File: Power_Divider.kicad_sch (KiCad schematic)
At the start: 31 parts, among them J8 Molex 73251-1153, J9 2118714-2, P10 CONUFL001-SMD-T, P11 CONUFL001-SMD-T, P12 CONUFL001-SMD-T, P9 CONUFL001-SMD-T, Q2 BSS138, U25 QPL9547, U26 RBP-140+

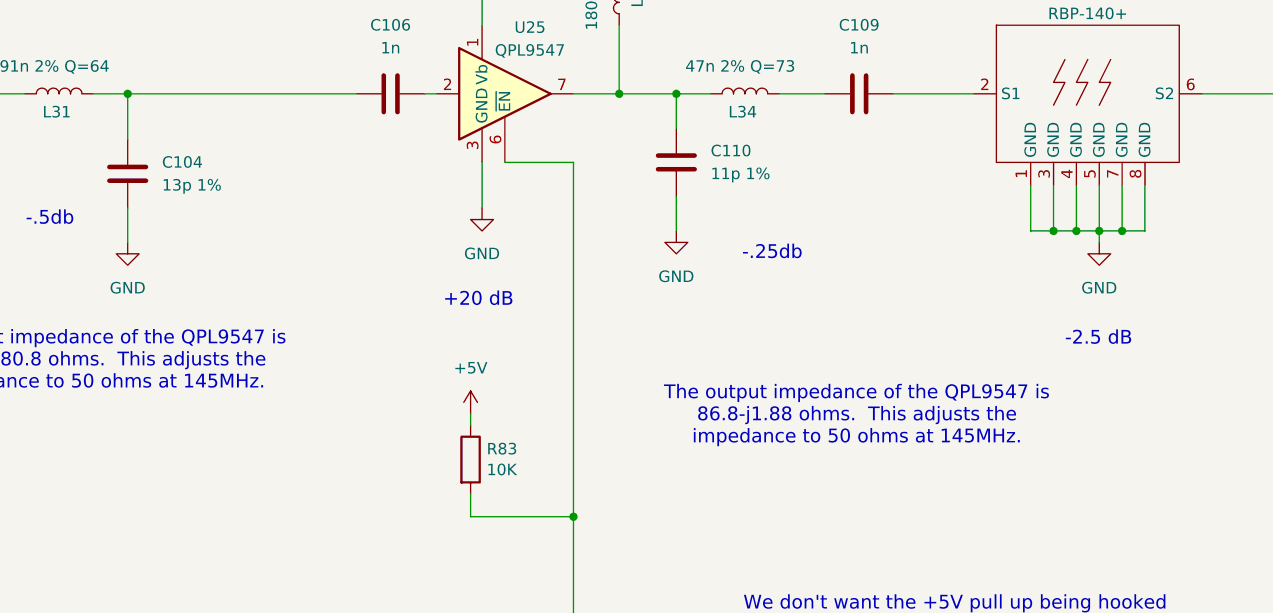
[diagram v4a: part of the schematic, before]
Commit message: More work on the LNA/PA impedance matchers
Did some simulations, found some issues.

Signed-off-by: Corey Minyard <corey@minyard.net>
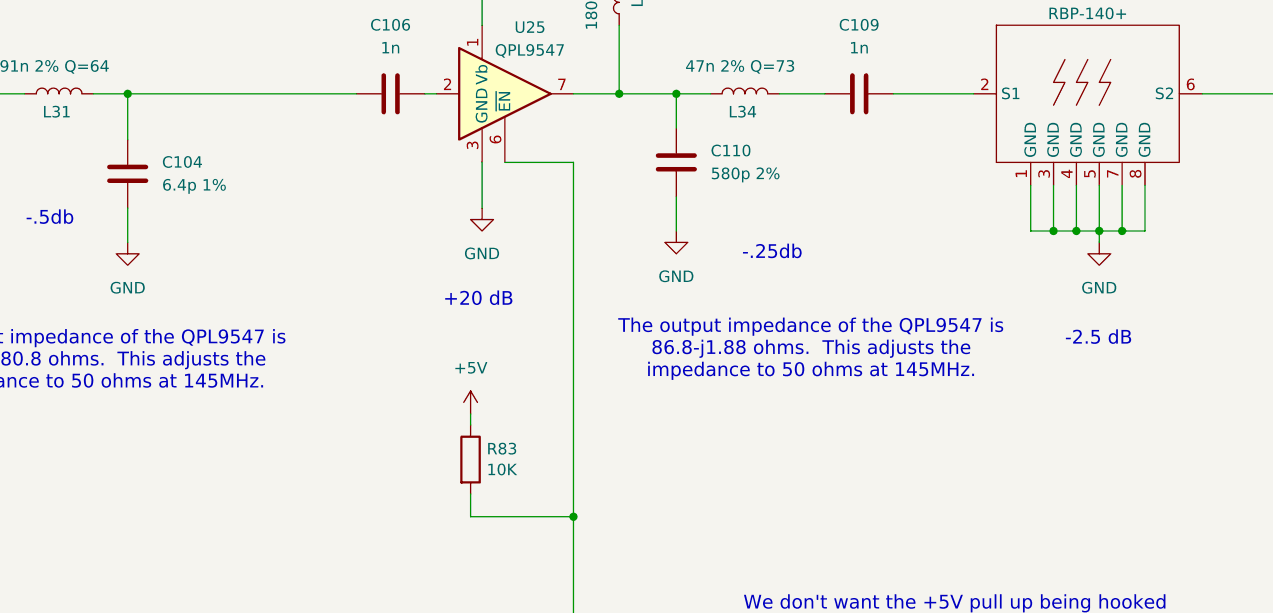
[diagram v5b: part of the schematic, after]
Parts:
- C104: value 13p 1% -> 6.4p 1%
- C110: value 11p 1% -> 580p 2%
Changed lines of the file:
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@@
 	(text "The output impedance of the QPL9547 is\n86.8-j1.88 ohms.  This adjusts the\nimpedance to 50 ohms at 145MHz."
 		(exclude_from_sim no)
-		(at 223.266 179.324 0)
+		(at 218.186 171.958 0)
 		(effects
 			(font
@@
 			)
 		)
-		(property "Value" "13p 1%"
+		(property "Value" "6.4p 1%"
 			(at 146.05 153.6699 0)
 			(effects
@@
 			)
 		)
-		(property "Value" "11p 1%"
+		(property "Value" "580p 2%"
 			(at 207.01 152.3999 0)
 			(effects

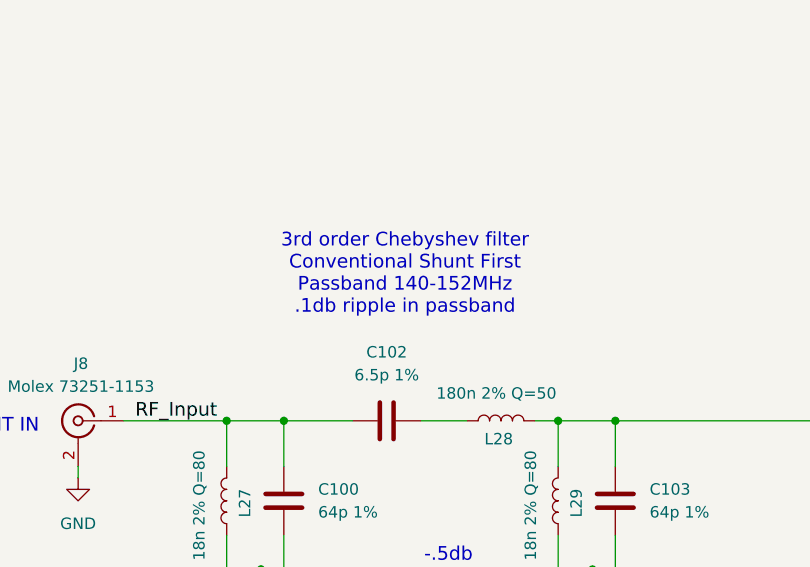
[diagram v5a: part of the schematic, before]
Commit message: Minor adjustments to values and impedance match simulation
Signed-off-by: Corey Minyard <corey@minyard.net>
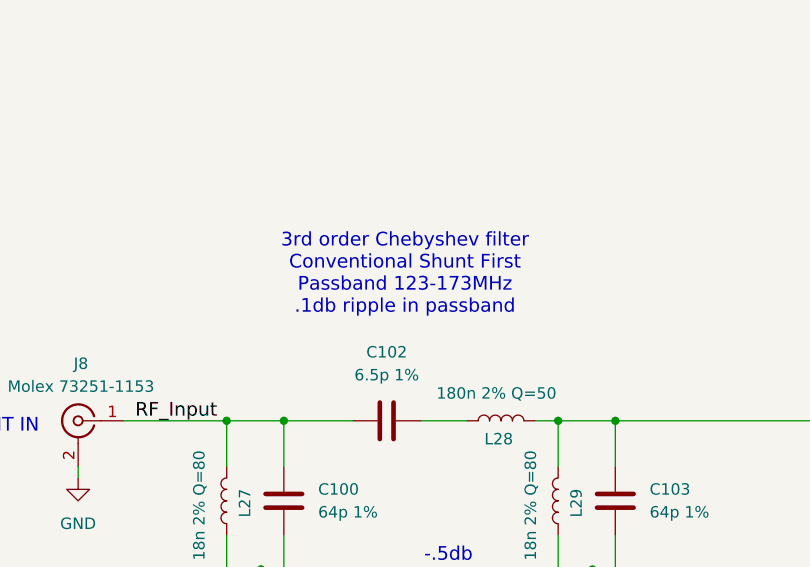
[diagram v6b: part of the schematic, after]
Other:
- note added: "3rd order Chebyshev filter Conventional Shunt First Passband 123-173MHz .1db ripple in passband"
- note removed: "3rd order Chebyshev filter Conventional Shunt First Passband 140-152MHz .1db ripple in passband"
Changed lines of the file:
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@@
 		)
 	)
-	(text "3rd order Chebyshev filter\nConventional Shunt First\nPassband 140-152MHz\n.1db ripple in passband\n"
+	(text "3rd order Chebyshev filter\nConventional Shunt First\nPassband 123-173MHz\n.1db ripple in passband\n"
 		(exclude_from_sim no)
 		(at 82.042 127.254 0)

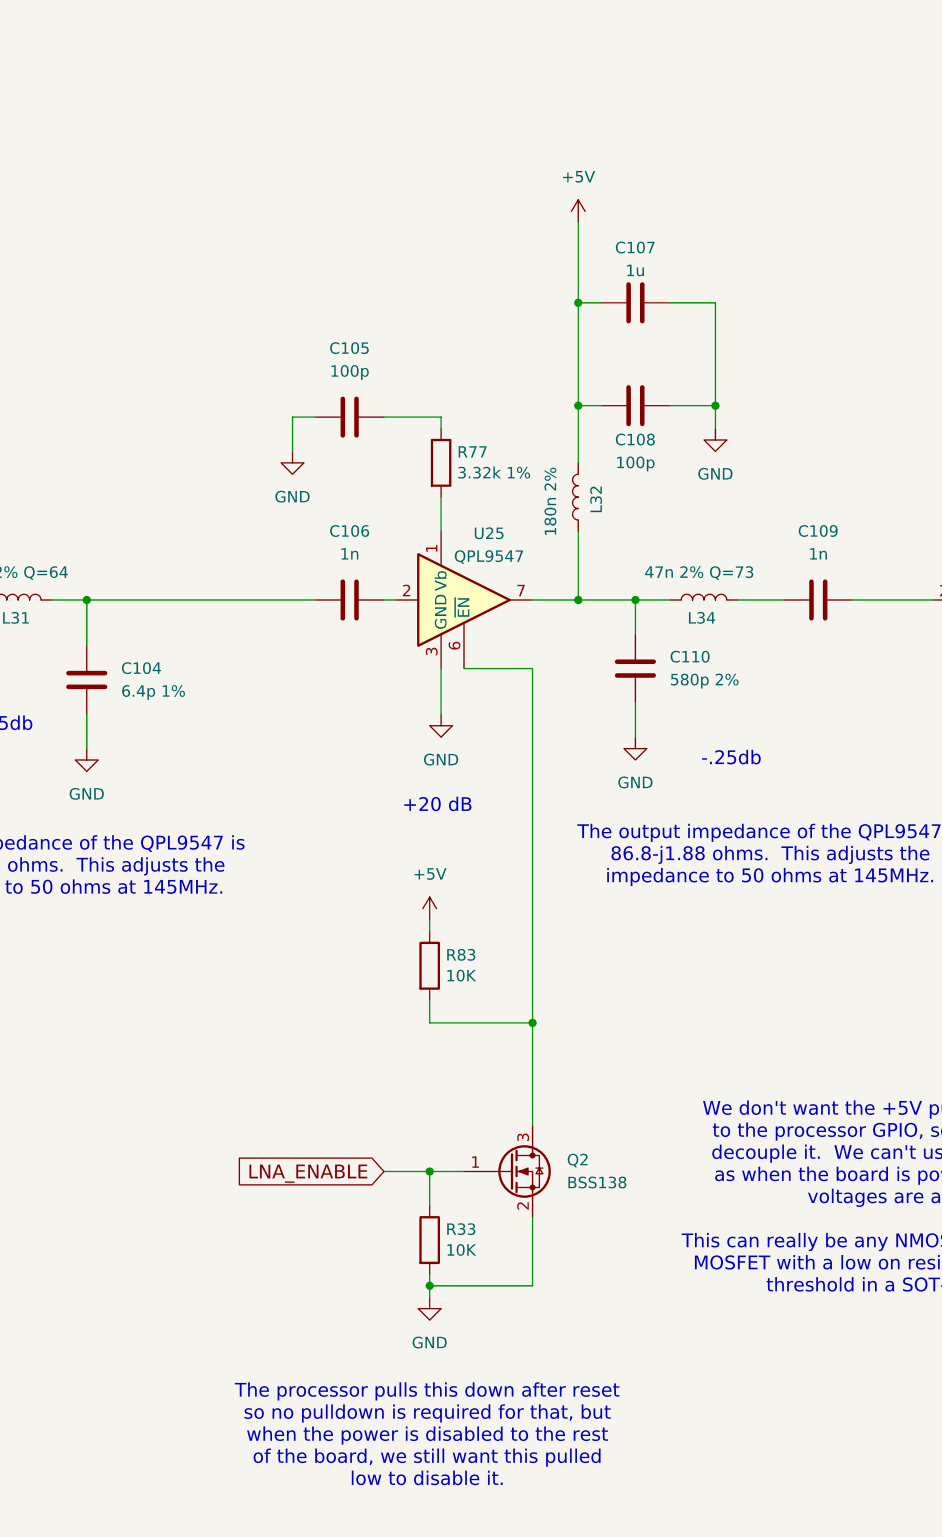
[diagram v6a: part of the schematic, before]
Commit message: Add 4 more MRAM parts
Signed-off-by: Corey Minyard <corey@minyard.net>
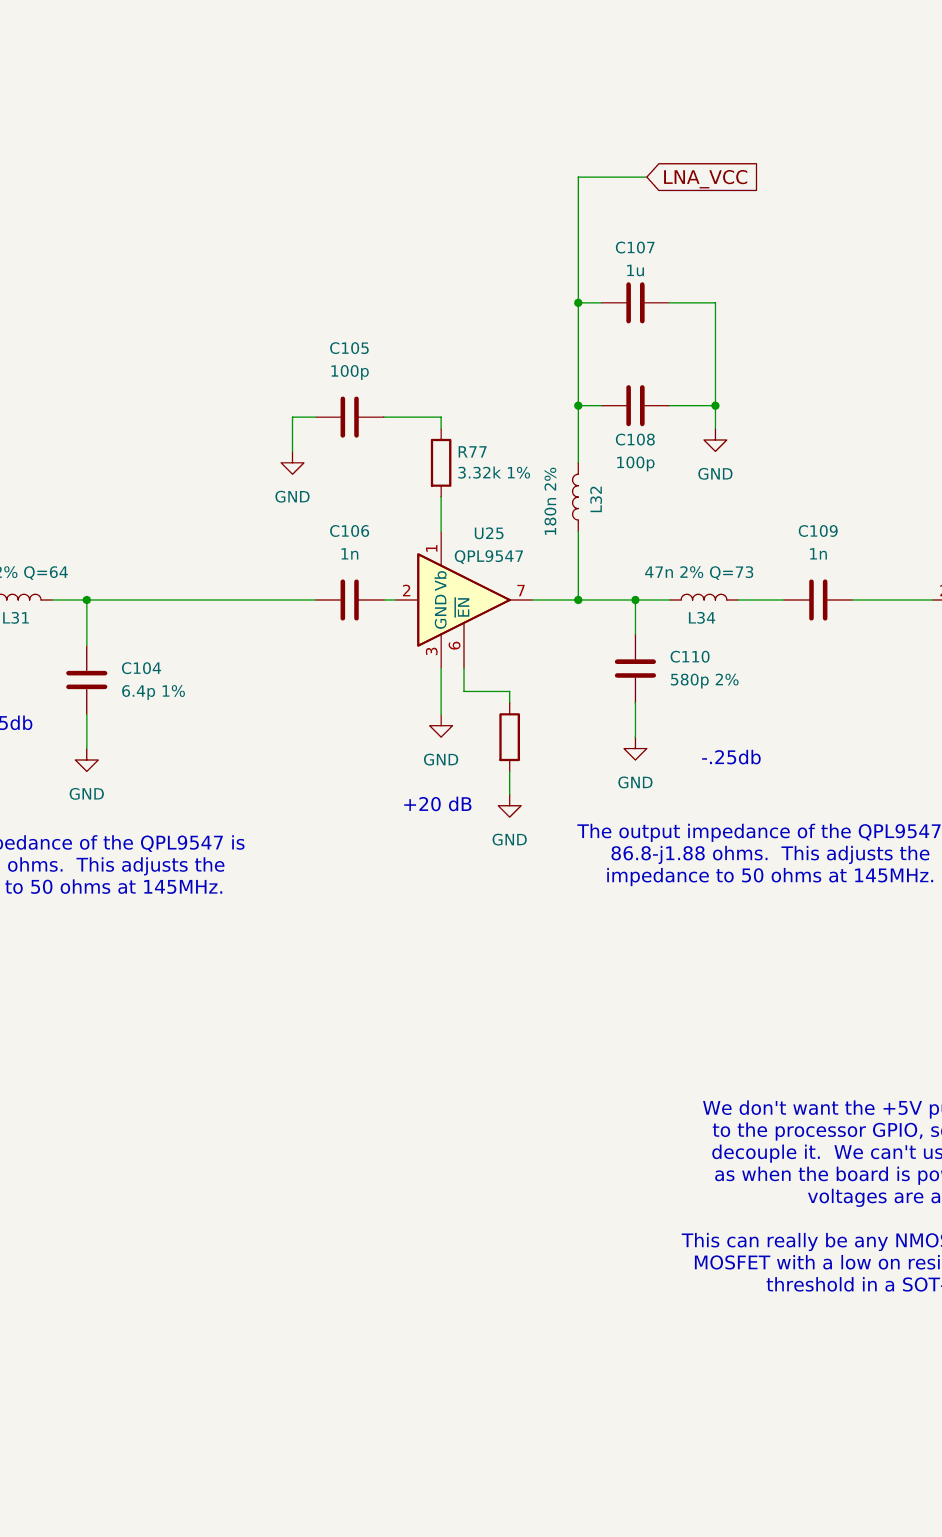
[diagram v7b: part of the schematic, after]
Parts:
- removed Q2: BSS138, Package_TO_SOT_SMD:SOT-23, symbol Transistor_FET:Q_NMOS_GSD
- removed R83: 10K, Resistor_SMD:R_0603_1608Metric_Pad0.98x0.95mm_HandSolder, symbol Device:R
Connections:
- net LNA_ENABLE is gone; now on an unnamed net: R33.1
- net +5V renamed LNA_VCC
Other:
- note removed: "The processor pulls this down after reset so no pulldown is required for that, but when the power is disabled to the rest of the board, we still want this pulled low to disable it."

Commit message: More work on various things
Signed-off-by: Corey Minyard <corey@minyard.net>
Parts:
- added H18, H19: Wire_Hole, PacSatDev_misc:Wire_Hole, symbol PACSAT_DEV_misc:CUBESAT_MOUNT_HOLE_1
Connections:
- net GND: now also H18.1, H19.1
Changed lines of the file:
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@@
 	)
 	(junction
+		(at 196.85 62.23)
+		(diameter 0)
+		(color 0 0 0 0)
+	)
+	(junction
 		(at 334.01 123.19)
 		(diameter 0)
@@
 	(wire
 		(pts
+			(xy 196.85 62.23) (xy 196.85 64.77)
+		)
+		(stroke
+			(width 0)
+			(type default)
+		)
+	)
+	(wire
+		(pts
 			(xy 361.95 123.19) (xy 361.95 148.59)
 		)
@@
 	(wire
 		(pts
+			(xy 181.61 53.34) (xy 196.85 53.34)
+		)
+		(stroke
+			(width 0)
+			(type default)
+		)
+	)
+	(wire
+		(pts
 			(xy 363.22 123.19) (xy 361.95 123.19)
 		)
@@
 	(wire
 		(pts
+			(xy 181.61 62.23) (xy 196.85 62.23)
+		)
+		(stroke
+			(width 0)
+			(type default)
+		)
+	)
+	(wire
+		(pts
 			(xy 99.06 50.8) (xy 104.14 50.8)
 		)
@@
 	(wire
 		(pts
+			(xy 196.85 53.34) (xy 196.85 62.23)
+		)
+		(stroke
+			(width 0)
+			(type default)
+		)
+	)
+	(wire
+		(pts
 			(xy 356.87 133.35) (xy 359.41 133.35)
 		)
@@
 	)
 	(symbol
+		(lib_id "PACSAT_DEV_misc:CUBESAT_MOUNT_HOLE_1")
+		(at 179.07 62.23 0)
+		(unit 1)
+		(exclude_from_sim no)
+		(in_bom yes)
+		(on_board yes)
+		(dnp no)
+		(property "Reference" "H19"
+			(at 179.8574 56.2102 0)
+			(effects
+				(font
+					(size 1.524 1.524)
+				)
+			)
+		)
+		(property "Value" "Wire_Hole"
+			(at 179.8574 58.9026 0)
+			(effects
+				(font
+					(size 1.524 1.524)
+				)
+			)
+		)
+		(property "Footprint" "PacSatDev_misc:Wire_Hole"
+			(at 179.07 62.23 0)
+			(effects
+				(font
+					(size 1.524 1.524)
+				)
+				(hide yes)
+			)
+		)
+		(property "Datasheet" ""
+			(at 179.07 62.23 0)
+			(effects
+				(font
+					(size 1.524 1.524)
+				)
+				(hide yes)
+			)
+		)
+		(property "Description" ""
+			(at 179.07 62.23 0)
+			(effects
+				(font
+					(size 1.27 1.27)
+				)
+			)
+		)
+		(pin "1"
+		)
+		(instances
+			(project "PacSat_AFSK"
+				(path "/cc9f42d2-6985-41ac-acab-5ab7b01c5b38/9af0eacb-5211-4e23-85d7-9c1805bbe6a4"
+					(reference "H19")
+					(unit 1)
+				)
+			)
+		)
+	)
+	(symbol
 		(lib_id "power:GND")
 		(at 283.21 80.01 0)
@@
 	)
 	(symbol
+		(lib_id "power:GND")
+		(at 196.85 64.77 0)
+		(unit 1)
+		(exclude_from_sim no)
+		(in_bom yes)
+		(on_board yes)
+		(dnp no)
+		(property "Reference" "#PWR0256"
+			(at 196.85 71.12 0)
+			(effects
+				(font
+					(size 1.27 1.27)
+				)
+				(hide yes)
+			)
+		)
+		(property "Value" "GND"
+			(at 196.977 69.1642 0)
+			(effects
+				(font
+					(size 1.27 1.27)
+				)
+			)
+		)
+		(property "Footprint" ""
+			(at 196.85 64.77 0)
+			(effects
+				(font
+					(size 1.27 1.27)
+				)
+				(hide yes)
+			)
+		)
+		(property "Datasheet" ""
+			(at 196.85 64.77 0)
+			(effects
+				(font
+					(size 1.27 1.27)
+				)
+				(hide yes)
+			)
+		)
+		(property "Description" ""
+			(at 196.85 64.77 0)
+			(effects
+				(font
+					(size 1.27 1.27)
+				)
+			)
+		)
+		(pin "1"
+		)
+		(instances
+			(project "PacSat_AFSK"
+				(path "/cc9f42d2-6985-41ac-acab-5ab7b01c5b38/9af0eacb-5211-4e23-85d7-9c1805bbe6a4"
+					(reference "#PWR0256")
+					(unit 1)
+				)
+			)
+		)
+	)
+	(symbol
 		(lib_id "PACSAT_DEV_misc:U_FL")
 		(at 284.48 71.12 0)
@@
 					(unit 1)
 				)
+			)
+		)
+	)
+	(symbol
+		(lib_id "PACSAT_DEV_misc:CUBESAT_MOUNT_HOLE_1")
+		(at 179.07 53.34 0)
+		(unit 1)
+		(exclude_from_sim no)
+		(in_bom yes)
+		(on_board yes)
+		(dnp no)
+		(property "Reference" "H18"
+			(at 179.8574 47.3202 0)
+			(effects
+				(font
+					(size 1.524 1.524)
+				)
+			)
+		)
+		(property "Value" "Wire_Hole"
+			(at 179.8574 50.0126 0)
+			(effects
+				(font
+					(size 1.524 1.524)
+				)
+			)
+		)
+		(property "Footprint" "PacSatDev_misc:Wire_Hole"
+			(at 179.07 53.34 0)
+			(effects
+				(font
+					(size 1.524 1.524)
+				)
+				(hide yes)
+			)
+		)
+		(property "Datasheet" ""
+			(at 179.07 53.34 0)
+			(effects
+				(font
+					(size 1.524 1.524)
+				)
+				(hide yes)
+			)
+		)
+		(property "Description" ""
+			(at 179.07 53.34 0)
+			(effects
+				(font
+					(size 1.27 1.27)
+				)
+			)
+		)
+		(pin "1"
+		)
+		(instances
+			(project "PacSat_AFSK"
+				(path "/cc9f42d2-6985-41ac-acab-5ab7b01c5b38/9af0eacb-5211-4e23-85d7-9c1805bbe6a4"
+					(reference "H18")
+					(unit 1)
+				)
